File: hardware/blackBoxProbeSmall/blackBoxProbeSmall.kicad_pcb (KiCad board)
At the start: 4 copper layers, 44 x 29 mm, 74 parts, among them J1 USB-ID, J2 JTAG_2X05, J3 JTAG_2X05, J4 Conn_01x04, Q1 Q_NMOS_DUAL, Q2 Q_PMOS_DUAL, U1 MCP1702-MB, U2 USBLC6-2, U3 STM32F103CBT, U4 74X2T45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

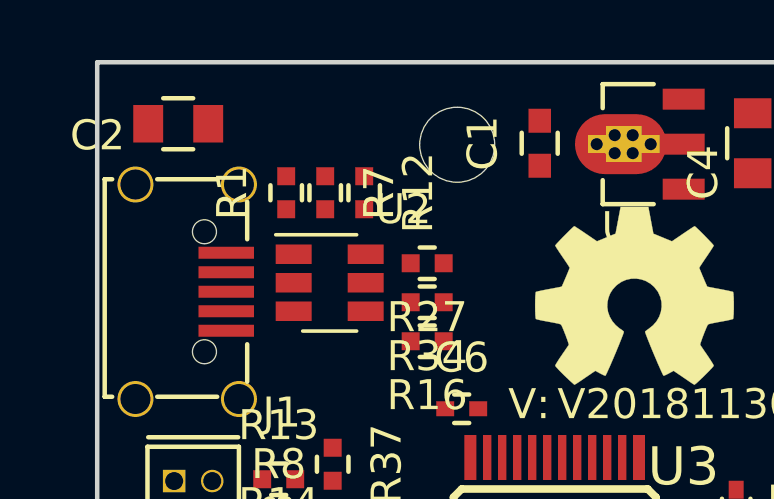
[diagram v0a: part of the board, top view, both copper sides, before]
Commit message: added fuse and updated 3d components
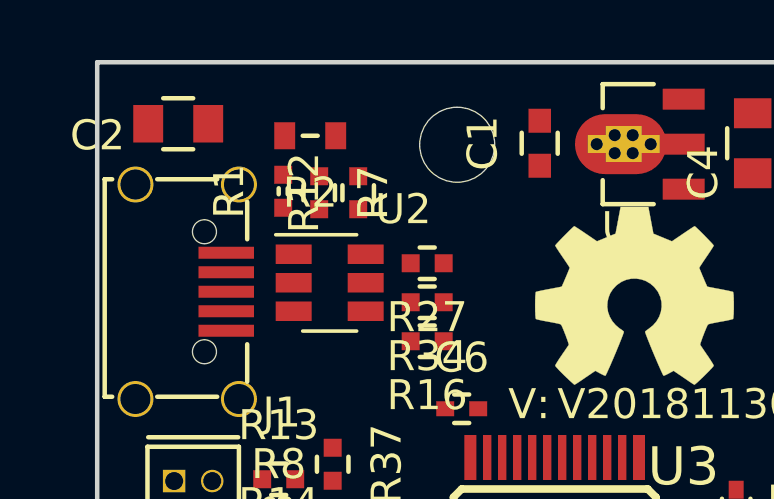
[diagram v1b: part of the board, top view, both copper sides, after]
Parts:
- added R2: FUSE, SquantorRcl:F_0603_hand, F.Cu at (130.8, 87.3)
- R1: footprint SquantorRcl:R_0402_hand -> SquantorRcl:L_0402_hand
- moved R7 0.20 mm to (131.1, 89.2)
- moved R12 0.20 mm to (132.4, 89.2), turned to 90 degrees
- moved R1 0.11 mm to (129.9, 89.2)
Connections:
- R1 pad 2: +5V -> Net-(R1-Pad2)
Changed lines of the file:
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@@
-(kicad_pcb (version 20171130) (host pcbnew 5.1.2-f72e74a~84~ubuntu18.04.1)
+(kicad_pcb (version 20171130) (host pcbnew 5.1.3-ffb9f22~84~ubuntu18.04.1)
   (general
     (thickness 1.6)
@@
     (tracks 0)
     (zones 0)
-    (modules 74)
-    (nets 64)
+    (modules 75)
+    (nets 65)
   )
   (page A4)
@@
   (net 62 "Net-(DA1-Pad3)")
   (net 63 "Net-(DA1-Pad4)")
+  (net 64 "Net-(R1-Pad2)")
   (net_class Default "This is the default net class."
     (clearance 0.127)
@@
     (add_net "Net-(J2-Pad4)")
     (add_net "Net-(J2-Pad6)")
+    (add_net "Net-(J2-Pad7)")
     (add_net "Net-(J2-Pad8)")
     (add_net "Net-(J3-Pad10)")
@@
     (add_net "Net-(J3-Pad4)")
     (add_net "Net-(J3-Pad6)")
+    (add_net "Net-(J3-Pad7)")
     (add_net "Net-(J3-Pad8)")
     (add_net "Net-(J4-Pad2)")
     (add_net "Net-(J4-Pad3)")
     (add_net "Net-(Q2-Pad1)")
+    (add_net "Net-(R1-Pad2)")
     (add_net "Net-(R16-Pad2)")
     (add_net "Net-(R27-Pad2)")
+    (add_net "Net-(U3-Pad10)")
+    (add_net "Net-(U3-Pad2)")
+    (add_net "Net-(U3-Pad27)")
+    (add_net "Net-(U3-Pad28)")
+    (add_net "Net-(U3-Pad3)")
+    (add_net "Net-(U3-Pad4)")
+    (add_net "Net-(U3-Pad43)")
+    (add_net "Net-(U3-Pad45)")
+    (add_net "Net-(U3-Pad46)")
     (add_net VDDA)
+  )
+  (module SquantorRcl:F_0603_hand (layer F.Cu)
+    (at 130.8 87.35 180)
+    (descr "Fuse SMD 0603, reflow soldering")
+    (tags "fuse 0603")
+    (attr smd)
+    (fp_text reference R2 (at 0 -1.9) (layer F.SilkS)
+      (effects (font (size 1 1) (thickness 0.15)))
+    )
+    (fp_text value FUSE (at 0 1.9) (layer F.Fab)
+      (effects (font (size 1 1) (thickness 0.15)))
+    )
+    (fp_line (start -0.25 0) (end 0.25 0) (layer F.SilkS) (width 0.15))
+    (fp_line (start 1.45 -0.75) (end 1.45 0.75) (layer F.CrtYd) (width 0.05))
+    (fp_line (start -1.45 -0.75) (end -1.45 0.75) (layer F.CrtYd) (width 0.05))
+    (fp_line (start -1.45 0.75) (end 1.45 0.75) (layer F.CrtYd) (width 0.05))
+    (fp_line (start -1.45 -0.75) (end 1.45 -0.75) (layer F.CrtYd) (width 0.05))
+    (fp_line (start -0.8 -0.4) (end 0.8 -0.4) (layer F.Fab) (width 0.1))
+    (fp_line (start 0.8 -0.4) (end 0.8 0.4) (layer F.Fab) (width 0.1))
+    (fp_line (start 0.8 0.4) (end -0.8 0.4) (layer F.Fab) (width 0.1))
+    (fp_line (start -0.8 0.4) (end -0.8 -0.4) (layer F.Fab) (width 0.1))
+    (pad 2 smd rect (at 0.85 0 180) (size 0.7 0.9) (layers F.Cu F.Paste F.Mask)
+      (net 64 "Net-(R1-Pad2)"))
+    (pad 1 smd rect (at -0.85 0 180) (size 0.7 0.9) (layers F.Cu F.Paste F.Mask)
+      (net 1 +5V))
+    (model ${KISYS3DMOD}/Resistor_SMD.3dshapes/R_0603_1608Metric.step
+      (at (xyz 0 0 0))
+      (scale (xyz 1 1 1))
+      (rotate (xyz 0 0 0))
+    )
+    (model ${KISYS3DMOD}/Inductor_SMD.3dshapes/L_0603_1608Metric.step
+      (at (xyz 0 0 0))
+      (scale (xyz 1 1 1))
+      (rotate (xyz 0 0 0))
+    )
+  )
+  (module SquantorRcl:L_0402_hand (layer F.Cu)
+    (at 129.9 89.2 90)
+    (descr "Inductor SMD 0402")
+    (tags "Inductor 0402")
+    (attr smd)
+    (fp_text reference R1 (at 0 -1.8 90) (layer F.SilkS)
+      (effects (font (size 1 1) (thickness 0.15)))
+    )
+    (fp_text value FB (at 0 1.8 90) (layer F.Fab)
+      (effects (font (size 1 1) (thickness 0.15)))
+    )
+    (fp_line (start -0.1 0.15) (end 0.1 0.15) (layer F.SilkS) (width 0.15))
+    (fp_line (start -0.1 -0.15) (end 0.1 -0.15) (layer F.SilkS) (width 0.15))
+    (fp_line (start 1.1 -0.55) (end 1.1 0.55) (layer F.CrtYd) (width 0.05))
+    (fp_line (start -1.1 -0.55) (end -1.1 0.55) (layer F.CrtYd) (width 0.05))
+    (fp_line (start -1.1 0.55) (end 1.1 0.55) (layer F.CrtYd) (width 0.05))
+    (fp_line (start -1.1 -0.55) (end 1.1 -0.55) (layer F.CrtYd) (width 0.05))
+    (fp_line (start -0.5 -0.25) (end 0.5 -0.25) (layer F.Fab) (width 0.1))
+    (fp_line (start 0.5 -0.25) (end 0.5 0.25) (layer F.Fab) (width 0.1))
+    (fp_line (start 0.5 0.25) (end -0.5 0.25) (layer F.Fab) (width 0.1))
+    (fp_line (start -0.5 0.25) (end -0.5 -0.25) (layer F.Fab) (width 0.1))
+    (pad 2 smd rect (at 0.55 0 90) (size 0.6 0.6) (layers F.Cu F.Paste F.Mask)
+      (net 64 "Net-(R1-Pad2)"))
+    (pad 1 smd rect (at -0.55 0 90) (size 0.6 0.6) (layers F.Cu F.Paste F.Mask)
+      (net 11 "Net-(J1-Pad1)"))
+    (model ${KISYS3DMOD}/Inductor_SMD.3dshapes/L_0402_1005Metric.step
+      (at (xyz 0 0 0))
+      (scale (xyz 1 1 1))
+      (rotate (xyz 0 0 0))
+    )
   )
   (module SquantorIC:SOT89-ViaTab-Microchip-MB (layer F.Cu)
@@
   )
   (module SquantorRcl:R_0402_hand (layer F.Cu)
-    (at 130 89.25 90)
-    (descr "Resistor SMD 0402, reflow soldering, Vishay (see dcrcw.pdf)")
-    (tags "resistor 0402")
-    (attr smd)
-    (fp_text reference R1 (at 0 -1.8 90) (layer F.SilkS)
-      (effects (font (size 1 1) (thickness 0.15)))
-    )
-    (fp_text value FB (at 0 1.8 90) (layer F.Fab)
-      (effects (font (size 1 1) (thickness 0.15)))
-    )
-    (fp_line (start -0.25 0.525) (end 0.25 0.525) (layer F.SilkS) (width 0.15))
-    (fp_line (start 0.25 -0.525) (end -0.25 -0.525) (layer F.SilkS) (width 0.15))
-    (fp_line (start 1.15 -0.65) (end 1.15 0.65) (layer F.CrtYd) (width 0.05))
-    (fp_line (start -1.15 -0.65) (end -1.15 0.65) (layer F.CrtYd) (width 0.05))
-    (fp_line (start -1.15 0.65) (end 1.15 0.65) (layer F.CrtYd) (width 0.05))
-    (fp_line (start -1.15 -0.65) (end 1.15 -0.65) (layer F.CrtYd) (width 0.05))
-    (fp_line (start -0.5 -0.25) (end 0.5 -0.25) (layer F.Fab) (width 0.1))
-    (fp_line (start 0.5 -0.25) (end 0.5 0.25) (layer F.Fab) (width 0.1))
-    (fp_line (start 0.5 0.25) (end -0.5 0.25) (layer F.Fab) (width 0.1))
-    (fp_line (start -0.5 0.25) (end -0.5 -0.25) (layer F.Fab) (width 0.1))
-    (pad 2 smd rect (at 0.55 0 90) (size 0.6 0.6) (layers F.Cu F.Paste F.Mask)
-      (net 1 +5V))
-    (pad 1 smd rect (at -0.55 0 90) (size 0.6 0.6) (layers F.Cu F.Paste F.Mask)
-      (net 11 "Net-(J1-Pad1)"))
-    (model ${KISYS3DMOD}/Resistor_SMD.3dshapes/R_0402_1005Metric.step
-      (at (xyz 0 0 0))
-      (scale (xyz 1 1 1))
-      (rotate (xyz 0 0 0))
-    )
-  )
-  (module SquantorRcl:R_0402_hand (layer F.Cu)
     (at 143.65 111.25)
     (descr "Resistor SMD 0402, reflow soldering, Vishay (see dcrcw.pdf)")
@@
   )
   (module SquantorRcl:R_0402_hand (layer F.Cu)
-    (at 131.3 89.25 270)
+    (at 131.1 89.25 270)
     (descr "Resistor SMD 0402, reflow soldering, Vishay (see dcrcw.pdf)")
     (tags "resistor 0402")
@@
   )
   (module SquantorRcl:R_0402_hand (layer F.Cu)
-    (at 132.6 89.25 270)
+    (at 132.4 89.25 90)
     (descr "Resistor SMD 0402, reflow soldering, Vishay (see dcrcw.pdf)")
     (tags "resistor 0402")
@@
     (fp_line (start 0.5 0.25) (end -0.5 0.25) (layer F.Fab) (width 0.1))
     (fp_line (start -0.5 0.25) (end -0.5 -0.25) (layer F.Fab) (width 0.1))
-    (pad 2 smd rect (at 0.55 0 270) (size 0.6 0.6) (layers F.Cu F.Paste F.Mask)
-      (net 2 GND))
-    (pad 1 smd rect (at -0.55 0 270) (size 0.6 0.6) (layers F.Cu F.Paste F.Mask)
+    (pad 2 smd rect (at 0.55 0 90) (size 0.6 0.6) (layers F.Cu F.Paste F.Mask)
+      (net 2 GND))
+    (pad 1 smd rect (at -0.55 0 90) (size 0.6 0.6) (layers F.Cu F.Paste F.Mask)
       (net 30 /USB_V))
     (model ${KISYS3DMOD}/Resistor_SMD.3dshapes/R_0402_1005Metric.step

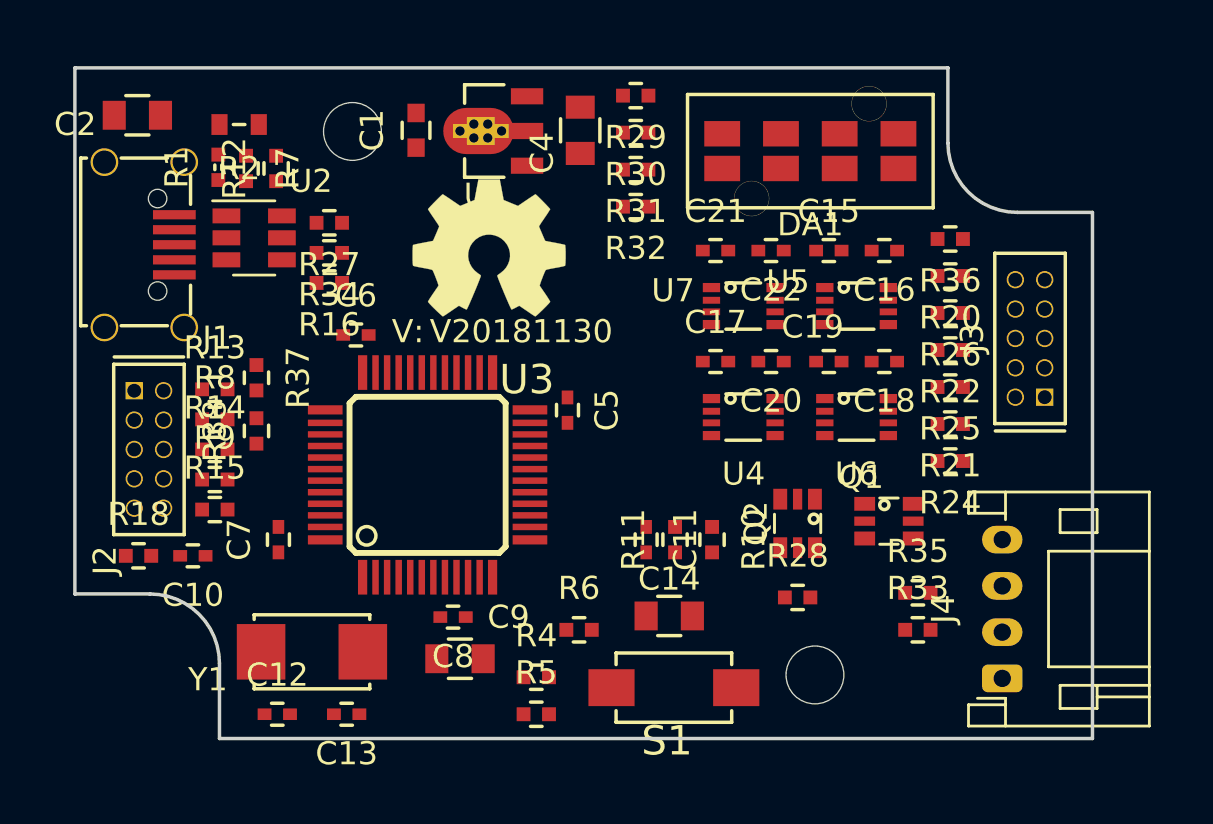
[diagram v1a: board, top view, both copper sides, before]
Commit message: reduced crystal size, replaced 0805 with 0603
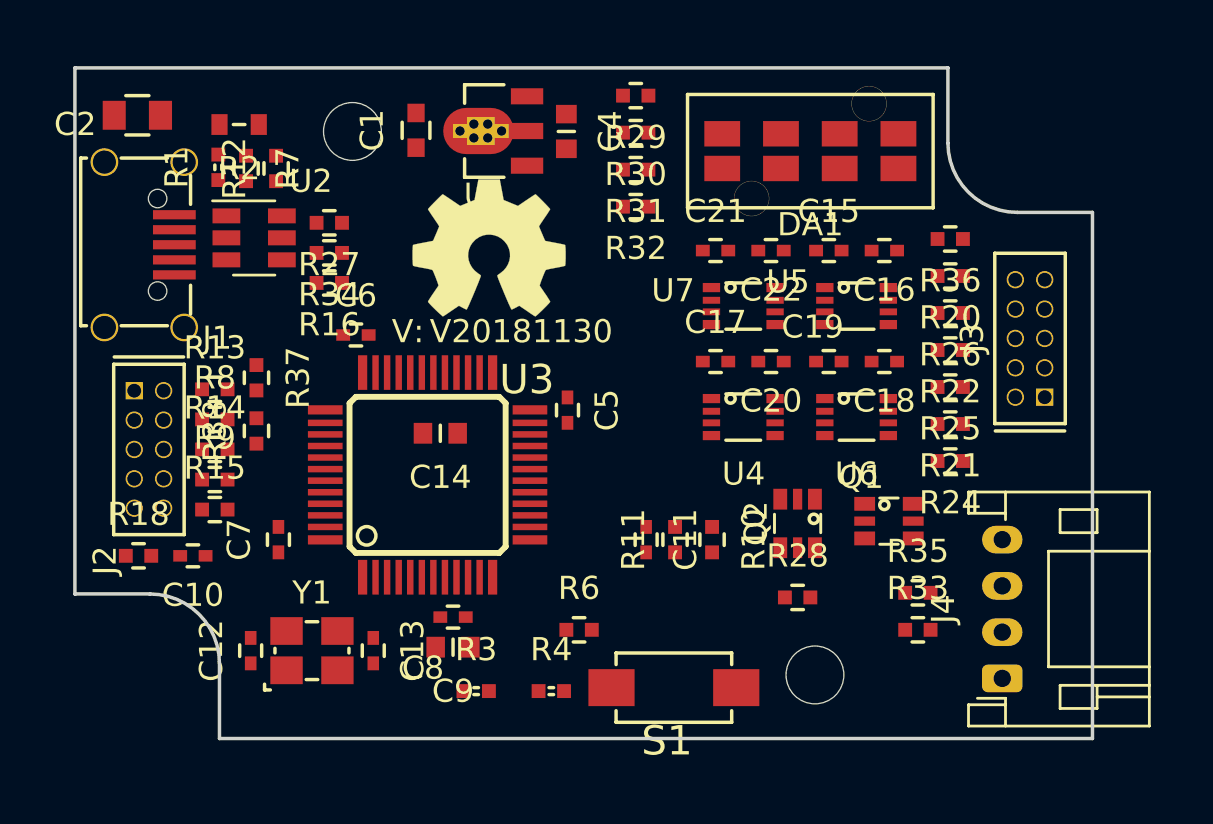
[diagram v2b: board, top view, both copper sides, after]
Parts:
- removed R5: R, SquantorRcl:R_0402_hand
- added R3: FB, SquantorRcl:L_0402_hand, F.Cu at (141.1, 111.8)
- C14, C4, C9: footprint SquantorRcl:C_0805 -> SquantorRcl:C_0603
- R4: value R -> FB; footprint SquantorRcl:R_0402_hand -> SquantorRcl:L_0402_hand
- Y1: value 8.000MHz -> 8MHz; footprint SquantorCrystal:X_5.0_3.2 -> SquantorCrystal:Crystal_3225_4
- moved C14 12.7 mm to (139.5, 100.7)
- moved C13 2.98 mm to (136.6, 110.1), turned to 270 degrees
- moved C12 2.98 mm to (131.3, 110.1), turned to 90 degrees
- moved R4 0.88 mm to (144.3, 111.8)
- moved C4 0.60 mm to (144.9, 87.7)
- moved C9 0.58 mm to (140.1, 110.0)
- moved Y1 0.05 mm to (133.9, 110.1)
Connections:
- R4 pad 1: VDDA -> +3V3
- R4 pad 2: +3V3 -> VDDA
- Y1 pad 2: Net-(C13-Pad1) -> GND

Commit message: imported changes into PCB to check 3d models
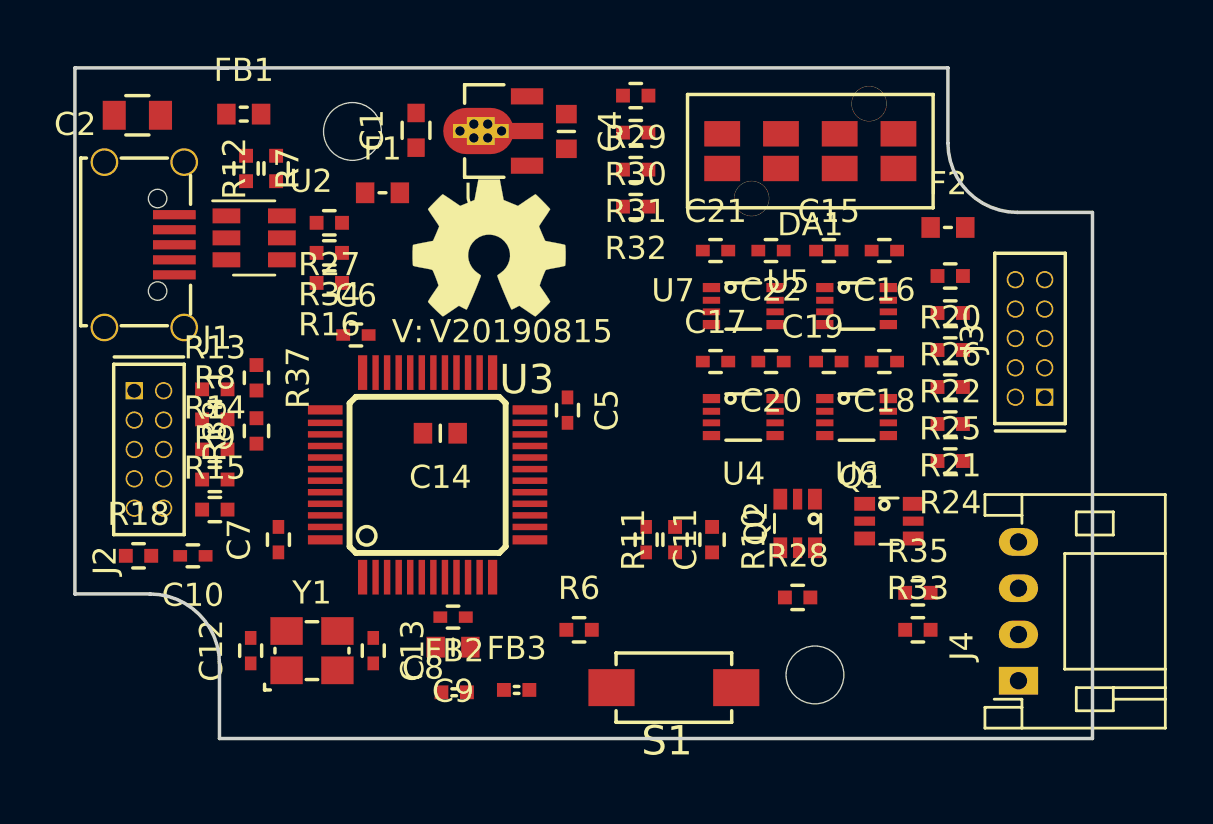
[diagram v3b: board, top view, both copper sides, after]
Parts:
- removed R1, R3, R4: FB, SquantorRcl:L_0402_hand
- removed R2: FUSE, SquantorRcl:F_0603_hand
- removed R36: 22, SquantorRcl:R_0402_hand
- added F1: 0.5A, SquantorRcl:F_0603_hand, F.Cu at (137.0, 90.3)
- added F2: 0.3A, SquantorRcl:F_0603_hand, F.Cu at (161.4, 91.8)
- added FB1: Ferrite_Bead, SquantorRcl:L_0603, F.Cu at (131.0, 86.9)
- added FB2: Ferrite_Bead, SquantorRcl:L_0402, F.Cu at (140.1, 111.9)
- added FB3: Ferrite_Bead, SquantorRcl:L_0402, F.Cu at (142.8, 111.8)
- C10, C15, C16, C17, C18, C19, C20, C21, C22, C5, C6, C7, C8: value 100n -> 1u
- J4: value Conn_01x04 -> DevBoardUartInput; footprint Connector_JST:JST_PH_S4B-PH-K_1x04_P2.00mm_Horizontal -> Connectors_JST:JST_PH_S4B-PH-K_04x2.00mm_Angled
- N2: value V20181130 -> V20190815
- moved J4 0.71 mm to (164.5, 111.4)
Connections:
- net GNDA renamed /VSSA
- net VDDA renamed /VDDA
- C1 pad 1: +5V -> /VUSB
- C1 pad 2: GND -> /VSS
- C10 pad 1: GND -> /VSS
- C12 pad 2: GND -> /VSS
- C13 pad 2: GND -> /VSS
- C14 pad 1: +3V3 -> /VDD
- C14 pad 2: GND -> /VSS
- C15 pad 1: +3V3 -> /VDD
- C15 pad 2: GND -> /VSS
- C16 pad 2: GND -> /VSS
- C17 pad 1: +3V3 -> /VDD
- C17 pad 2: GND -> /VSS
- C18 pad 2: GND -> /VSS
- C19 pad 1: +3V3 -> /VDD
- C19 pad 2: GND -> /VSS
- C2 pad 1: GND -> /VSS
- C20 pad 2: GND -> /VSS
- C21 pad 1: +3V3 -> /VDD
- C21 pad 2: GND -> /VSS
- C22 pad 2: GND -> /VSS
- C4 pad 1: +3V3 -> /VDD
- C4 pad 2: GND -> /VSS
- C5 pad 1: +3V3 -> /VDD
- C5 pad 2: GND -> /VSS
- C6 pad 1: +3V3 -> /VDD
- C6 pad 2: GND -> /VSS
- C7 pad 1: +3V3 -> /VDD
- C7 pad 2: GND -> /VSS
- DA1 pad 5: GND -> /VSS
- DA1 pad 6: GND -> /VSS
- DA1 pad 7: GND -> /VSS
- DA1 pad 8: GND -> /VSS
- J1 pad 4: GND -> /VSS
- J1 pad 5: GND -> /VSS
- J2 pad 1: +3V3 -> /VDD
- J2 pad 3: GND -> /VSS
- J2 pad 5: GND -> /VSS
- J2 pad 7: (no net) -> Net-(J2-Pad7)
- J2 pad 9: GND -> /VSS
- J3 pad 7: (no net) -> Net-(J3-Pad7)
- J4 pad 1: /PROBE_VDD -> GND
- J4 pad 2: Net-(J4-Pad2) -> /PROBE_VDD
- J4 pad 4: GND -> Net-(J4-Pad4)
- R12 pad 2: GND -> /VSS
- R18 pad 1: +3V3 -> /VDD
- R29 pad 2: +3V3 -> /VDD
- R33 pad 1: Net-(J4-Pad2) -> Net-(J4-Pad3)
- R33 pad 2: /PROBE_E_TX -> /PROBE_E_RX
- R35 pad 1: Net-(J4-Pad3) -> Net-(J4-Pad4)
- R35 pad 2: /PROBE_E_RX -> /PROBE_E_TX
- R37 pad 1: +3V3 -> /VDD
- R38 pad 1: GND -> /VSS
- R6 pad 1: +3V3 -> /VDD
- R7 pad 1: +5V -> /VUSB
- S1 pad 1: GND -> /VSS
- U1 pad 1: GND -> /VSS
- U1 pad 2: +5V -> /VUSB
- U1 pad 3: +3V3 -> /VDD
- U1 pad TAB: +5V -> (no net)
- U3 pad 1: +3V3 -> /VDD
- U3 pad 10: (no net) -> Net-(U3-Pad10)
- U3 pad 2: (no net) -> Net-(U3-Pad2)
- U3 pad 23: GND -> /VSS
- U3 pad 24: +3V3 -> /VDD
- U3 pad 27: (no net) -> Net-(U3-Pad27)
- U3 pad 28: (no net) -> Net-(U3-Pad28)
- U3 pad 3: (no net) -> Net-(U3-Pad3)
- U3 pad 35: GND -> /VSS
- U3 pad 36: +3V3 -> /VDD
- U3 pad 4: (no net) -> Net-(U3-Pad4)
- U3 pad 40: +3V3 -> /VDD
- U3 pad 41: +3V3 -> /VDD
- U3 pad 42: +3V3 -> /VDD
- U3 pad 43: (no net) -> Net-(U3-Pad43)
- U3 pad 44: GND -> /VSS
- U3 pad 45: (no net) -> Net-(U3-Pad45)
- U3 pad 46: (no net) -> Net-(U3-Pad46)
- U3 pad 47: GND -> /VSS
- U3 pad 48: +3V3 -> /VDD
- U4 pad 1: +3V3 -> /VDD
- U4 pad 2: GND -> /VSS
- U4 pad 4: GND -> /VSS
- U4 pad 5: +3V3 -> /VDD
- U4 pad 7: GND -> /VSS
- U5 pad 1: +3V3 -> /VDD
- U5 pad 4: GND -> /VSS
- U5 pad 5: +3V3 -> /VDD
- U6 pad 1: +3V3 -> /VDD
- U6 pad 4: GND -> /VSS
- U6 pad 5: GND -> /VSS
- U7 pad 1: +3V3 -> /VDD
- U7 pad 2: GND -> /VSS
- U7 pad 4: GND -> /VSS
- U7 pad 7: GND -> /VSS
- Y1 pad 2: GND -> /VSS
- Y1 pad 4: GND -> /VSS

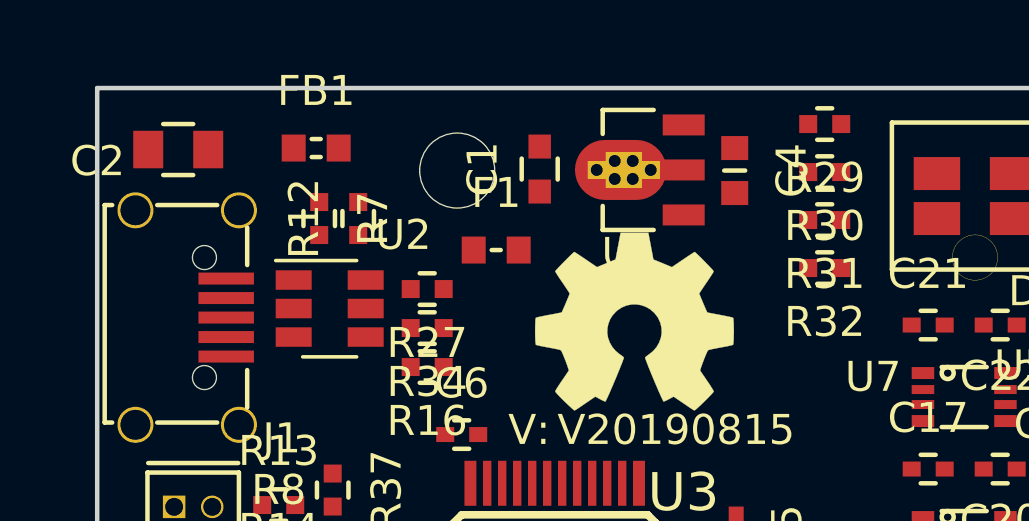
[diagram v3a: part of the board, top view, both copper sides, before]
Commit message: updated nets to non global ones
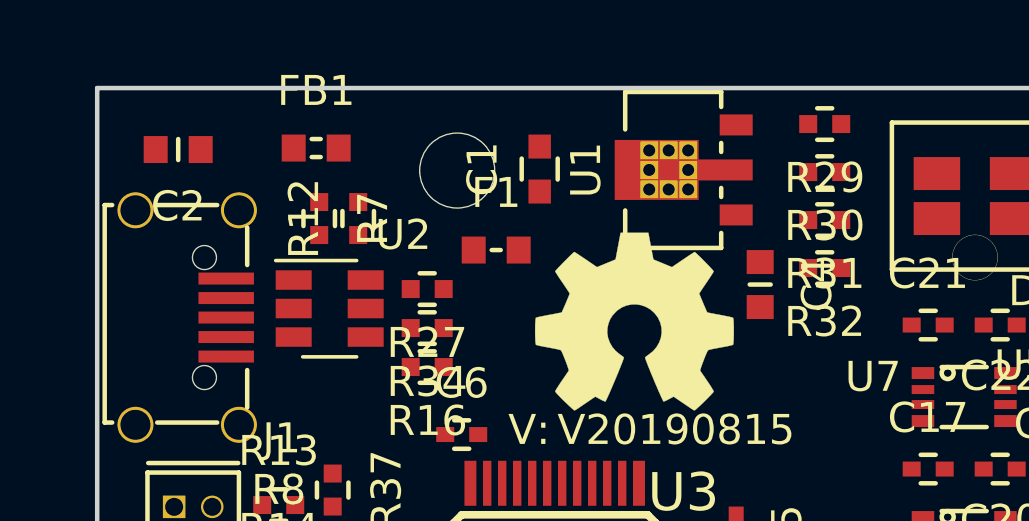
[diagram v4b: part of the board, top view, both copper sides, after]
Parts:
- C2: footprint SquantorRcl:C_0805 -> SquantorRcl:C_0603
- U1: footprint SquantorIC:SOT89-ViaTab-Microchip-MB -> SquantorIC:SOT89-NXP-Viatab
- moved C4 3.89 mm to (145.8, 91.5)
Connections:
- C11 pad 1: GND -> /VSS
- F2 pad 2: /PROBE_E_VDD -> Net-(F2-Pad2)
- J3 pad 3: GND -> /VSS
- J3 pad 5: GND -> /VSS
- J3 pad 9: GND -> /VSS
- J4 pad 1: GND -> /VSS
- Q1 pad 1: GND -> /VSS
- Q1 pad 4: GND -> /VSS
- Q2 pad 3: /PROBE_VDD -> Net-(F2-Pad2)
- Q2 pad 6: +3V3 -> /VDD
- R11 pad 2: GND -> /VSS
- U2 pad 2: GND -> /VSS
- U2 pad 5: +5V -> /VUSB
- U4 pad 8: /PROBE_E_VDD -> /PROBE_VDD
- U5 pad 8: /PROBE_E_VDD -> /PROBE_VDD
- U6 pad 8: /PROBE_E_VDD -> /PROBE_VDD
- U7 pad 8: /PROBE_E_VDD -> /PROBE_VDD
